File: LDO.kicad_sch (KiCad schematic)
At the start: 3 parts, among them U3 LD39150DT33-R

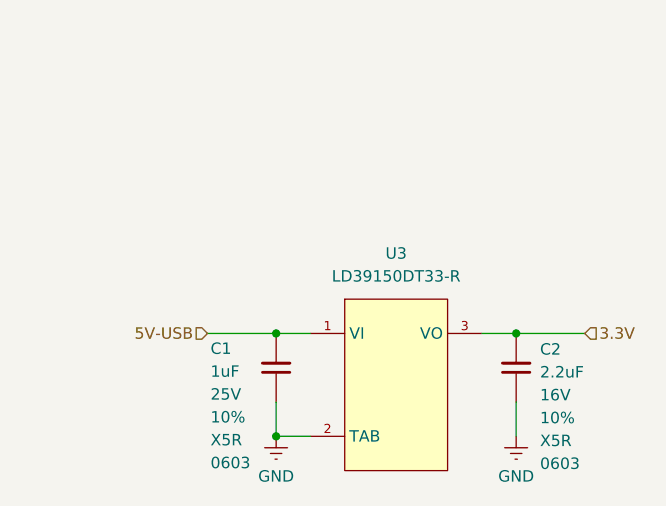
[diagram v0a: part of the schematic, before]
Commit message: adjusted capacitor params
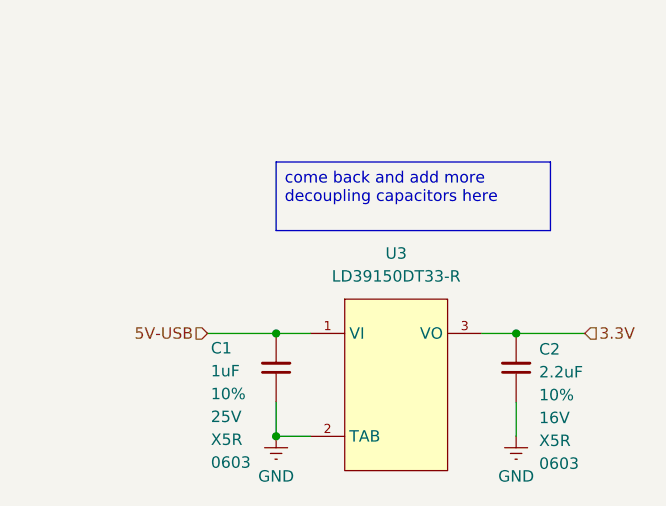
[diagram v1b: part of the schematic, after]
